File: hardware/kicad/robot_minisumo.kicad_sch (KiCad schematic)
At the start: 0 parts

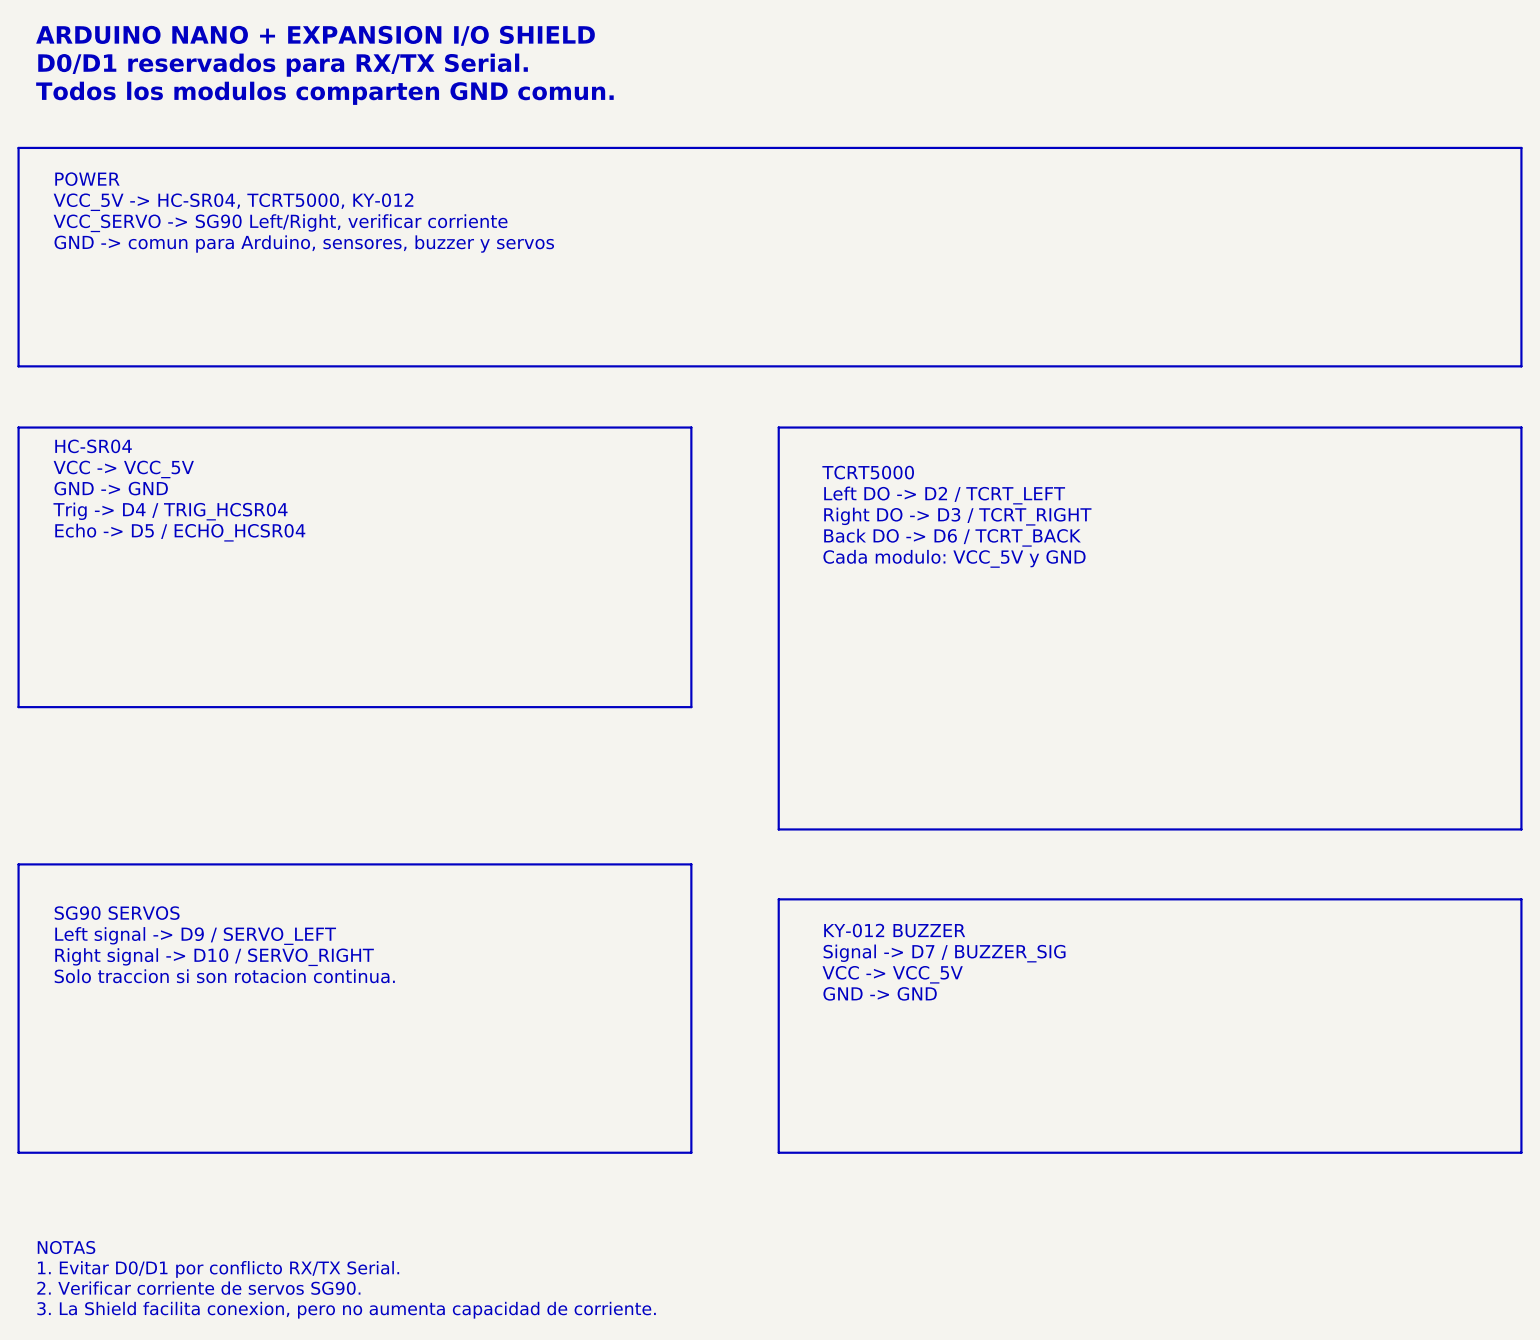
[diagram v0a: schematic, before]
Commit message: Align firmware and docs with tested TCRT pinout
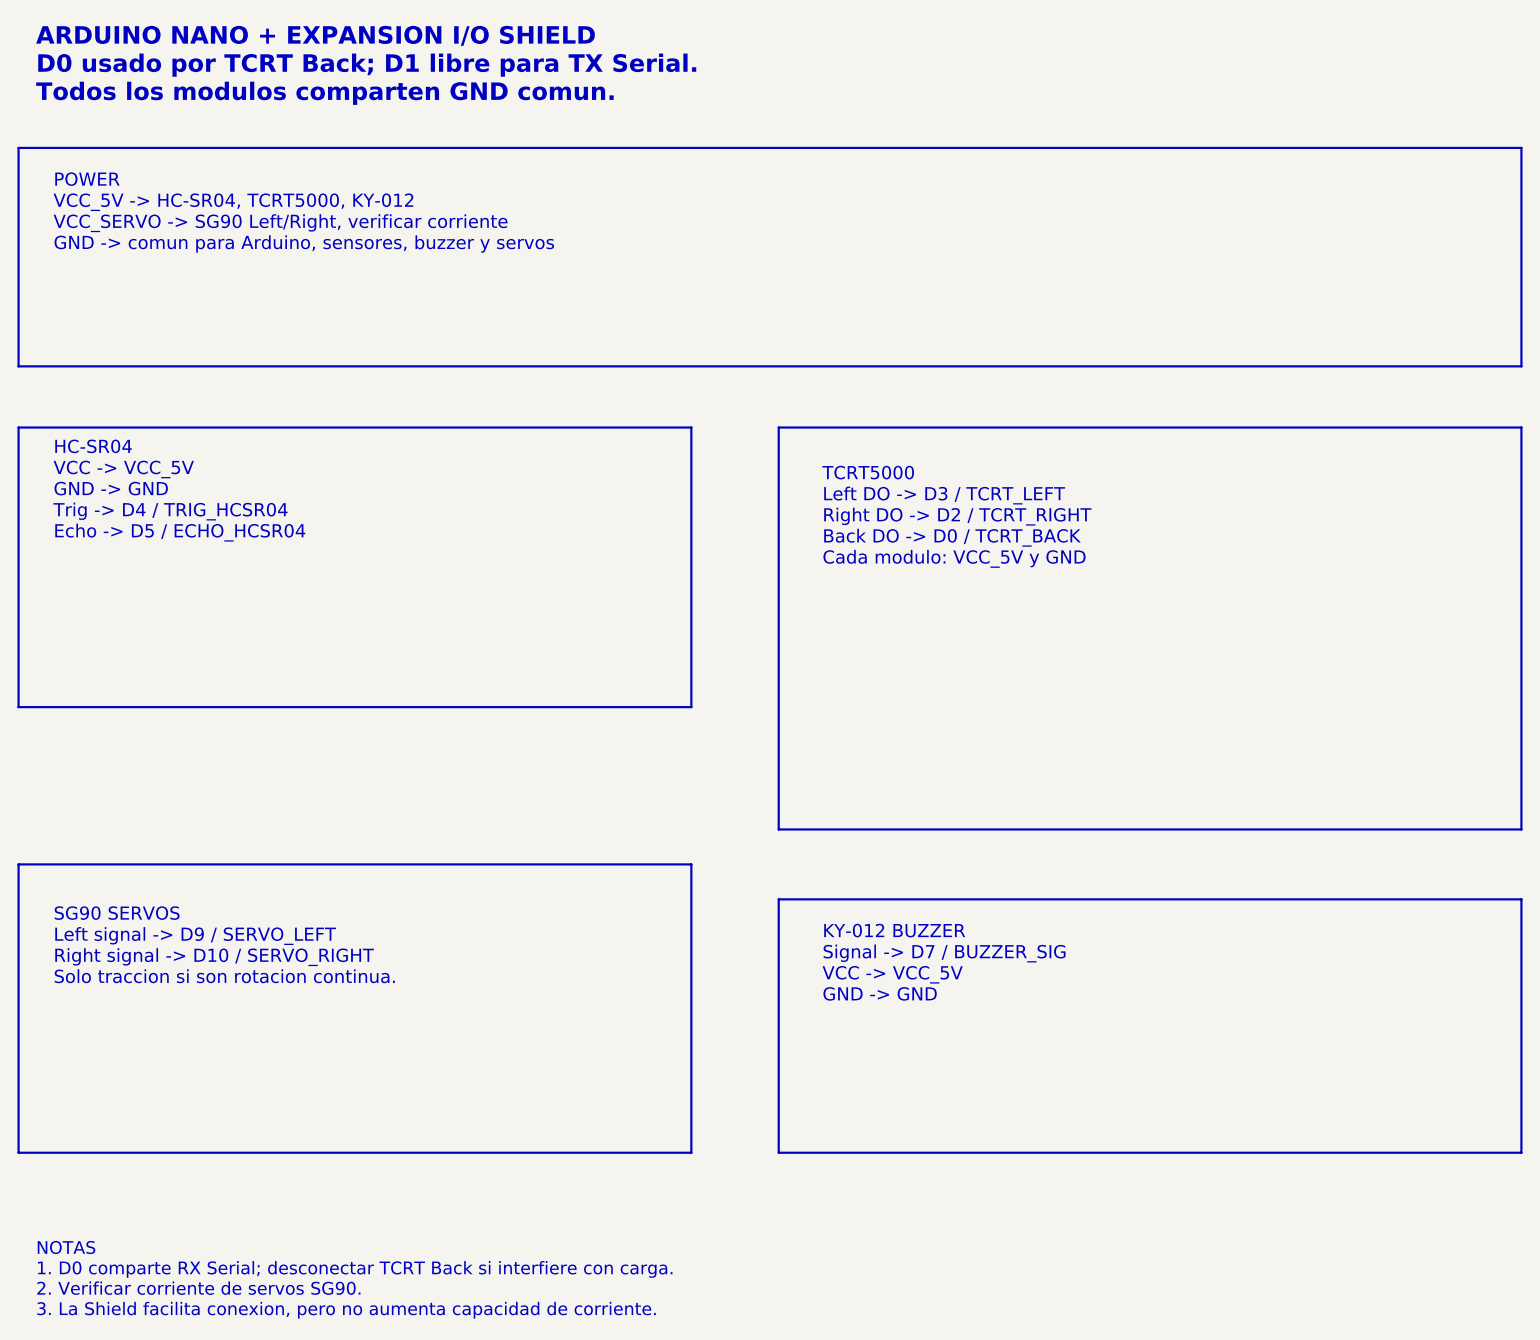
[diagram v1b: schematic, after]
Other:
- note added: "ARDUINO NANO + EXPANSION I/O SHIELD D0 usado por TCRT Back; D1 libre para TX Serial. Todos los modulos comparten GND comun."
- note added: "NOTAS 1. D0 comparte RX Serial; desconectar TCRT Back si interfiere con carga. 2. Verificar corriente de servos SG90. 3. La Shield facilita conexion, pero no aumenta capacidad de corriente."
- note added: "TCRT5000 Left DO -> D3 / TCRT_LEFT Right DO -> D2 / TCRT_RIGHT Back DO -> D0 / TCRT_BACK Cada modulo: VCC_5V y GND"
- note removed: "ARDUINO NANO + EXPANSION I/O SHIELD D0/D1 reservados para RX/TX Serial. Todos los modulos comparten GND comun."
- note removed: "NOTAS 1. Evitar D0/D1 por conflicto RX/TX Serial. 2. Verificar corriente de servos SG90. 3. La Shield facilita conexion, pero no aumenta capacidad de corriente."
- note removed: "TCRT5000 Left DO -> D2 / TCRT_LEFT Right DO -> D3 / TCRT_RIGHT Back DO -> D6 / TCRT_BACK Cada modulo: VCC_5V y GND"
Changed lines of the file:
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@@
     (date "2026-06-05")
     (rev "1.1")
-    (comment 1 "Pinout seguro sin D0/D1")
+    (comment 1 "Pinout real probado TCRT D3/D2/D0")
     (comment 2 "No PCB personalizada; montaje sobre Shield")
   )
-  (text "ARDUINO NANO + EXPANSION I/O SHIELD\nD0/D1 reservados para RX/TX Serial.\nTodos los modulos comparten GND comun."
+  (text "ARDUINO NANO + EXPANSION I/O SHIELD\nD0 usado por TCRT Back; D1 libre para TX Serial.\nTodos los modulos comparten GND comun."
     (at 20 25 0)
     (effects (font (size 2 2) (bold yes)) (justify left bottom))
@@
     (stroke (width 0.25) (type solid)) (fill (type none))
   )
-  (text "TCRT5000\nLeft DO -> D2 / TCRT_LEFT\nRight DO -> D3 / TCRT_RIGHT\nBack DO -> D6 / TCRT_BACK\nCada modulo: VCC_5V y GND"
+  (text "TCRT5000\nLeft DO -> D3 / TCRT_LEFT\nRight DO -> D2 / TCRT_RIGHT\nBack DO -> D0 / TCRT_BACK\nCada modulo: VCC_5V y GND"
     (at 110 78 0)
     (effects (font (size 1.5 1.5)) (justify left bottom))
@@
     (effects (font (size 1.5 1.5)) (justify left bottom))
   )
-  (text "NOTAS\n1. Evitar D0/D1 por conflicto RX/TX Serial.\n2. Verificar corriente de servos SG90.\n3. La Shield facilita conexion, pero no aumenta capacidad de corriente."
+  (text "NOTAS\n1. D0 comparte RX Serial; desconectar TCRT Back si interfiere con carga.\n2. Verificar corriente de servos SG90.\n3. La Shield facilita conexion, pero no aumenta capacidad de corriente."
     (at 20 164 0)
     (effects (font (size 1.45 1.45)) (justify left bottom))
